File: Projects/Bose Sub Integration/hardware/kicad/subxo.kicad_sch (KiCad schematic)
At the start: 44 parts, among them J1 IN L, J2 IN R, J3 OUT 3.5mm, J4 PWR IN 15V, J5 POLARITY SW, J6 LEVEL POT 10k, J7 INV LED, U1 TL074, U2 LM7812

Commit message: Sub crossover: redraw the schematic so it can be read
The schematic was electrically correct and visually useless: every one of its
112 wires was exactly 2.54 mm, one stub per pin, each ending in a net label.
Nothing was drawn as a connection, so tracing a net meant text-searching the
sheet, and the Sallen-Key and the op-amp stages were unrecognisable.

Redrawn in blocks with real wires, ground symbols and drawn feedback loops:
power in, status LEDs and virtual ground across the top; inputs, summing,
Sallen-Key and polarity inverter through the middle; output stage and the tied
-off spare section below.

The electrical design is untouched and provably so - the netlist partition,
all 44 parts, 31 nets and 112 nodes, is identical, and Value/Footprint are
copied from the old sheet rather than retyped. Net names are preserved too,
since the PCB matches on them; the one exception is /GND -> GND, because
ground moved from a text label onto proper power symbols.

  stitched pins   97% -> 8%       median wire  2.54 mm -> 10.16 mm
  wired pins      13% -> 92%      junctions          0 -> 34
  ERC violations     9 -> 5       ground symbols     0 -> 9

tools/subxo_layout.py regenerates the sheet, so the drawing is reproducible.
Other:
- note added: "A POWER IN +15 V -> LM7812 -> +12 V"
- note added: "An unterminated spare section oscillates and couples into its neighbours through the shared supply."
- note added: "B STATUS LEDS"
- note added: "C VIRTUAL GROUND +6 V, buffered"
- note added: "D INPUTS L + R, DC-blocked, summed"
- note added: "D2 is lit from J7 by the polarity switch's spare pole."
- note added: "E SALLEN-KEY LOW-PASS 2nd order"
- note added: "F POLARITY INVERTER unity gain -1"
- note added: "G OUTPUT polarity select -> level -> jack"
- note added: "H SPARE SECTION tied off, not floating"
- note added: "JP1/JP2 select C1 and C2 independently -- nine corners, not three."
- note added: "LK1 is the single tie between supply return and signal ground."
- note added: "R7 + JP3 let the output shield be damped or lifted at the jack."
- note added: "R_b1/R_b2 are the only DC path to U1A's + input -- without them the amp drifts to a rail."
- note added: "U1 supply: pin 4 = V12, pin 11 = GND."
- note removed: "A POWER IN -> +12 V"
- note removed: "A4 is the spare section: + on VGND, out tied to in-. An unterminated spare oscillates and couples into its neighbours through the shared supply."
- note removed: "B U1 SUPPLY"
- note removed: "Bose Companion 5 sub crossover -- mono-summing 2nd-order Sallen-Key low-pass."
- note removed: "C VIRTUAL GROUND 6 V"
- note removed: "C1 returns to N1 -- the Sallen-Key feedback path. Not N2. JP1 selects C1 (odd pin = cap, even pin = N1); JP2 selects C2 (odd = cap, even = VGND). They select INDEPENDENTLY -- nine corners, not three pairs. Corners below are MEASURED on the rev A board, not calculated: the quoted f0 = 1/(2*pi*R*sqrt(C1*C2)) is not a -3 dB point, and C_in sits inside the filter. See Results - Sub Crossover Bring-up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"
- note removed: "C_in1/C_in2 use a dual-pitch footprint: 5.00 mm for the 220n as built (or a 2u2 non-polarised electrolytic), 15.00 mm for a real 2u2 film part. Fit ONE pair. 220n puts ~8.8k of reactance in series with R1 at 82 Hz, so it is part of the filter, not just an input high-pass -- it costs 1.3-3.1 dB of passband level and damps the peaking. Whether that is a defect or a feature is a listening question; 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"
- note removed: "C_out + faces SW_COM: that node sits at 6 V DC, the pot side at 0 V. J6 pin 3 = GND, not VGND -- C_out has already removed the 6 V bias; referencing the pot to VGND would thump the driver at power-on. JP3 shorts R7 (ground lift). Normally fitted."
- note removed: "D INPUT L"
- note removed: "D1 = power lamp on V12 (proves the LM7812, not just VIN). D2 = INVERTED lamp, fed from SW2's unused second pole via J7. Both ~2 mA. No LED touches a signal node."
- note removed: "E INPUT R"
- note removed: "F SALLEN-KEY LOW-PASS"
- note removed: "G POLARITY INVERTER"
- note removed: "H OUTPUT STAGE"
- note removed: "I STATUS LEDS"
- note removed: "Off-board: level pot (J6), polarity switch (J5), all panel jacks (J1/J2/J3). Process: single-sided THT, bottom copper only, board outline 100 x 100 mm. Copper is isolation-milled on the CNC with an 0.8 mm flat end mill; the fiber laser does the silkscreen only. Routing clearance 0.85 mm / track 1.0 mm. The 0.8 mm tool width is a hard floor on every copper-to-copper gap. Fixed-pitch pads sit below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"
- note removed: "R_b1/R_b2 are the only DC path to A1's + input (C_in blocks DC, C2 is a capacitor). Without them A1 drifts to a rail. They sit after the coupling caps -- 100k at N1 would shift every corner by 8%."
- note removed: "Reference names vs the handoff document: KiCad treats a reference with no trailing digit as unannotated, so C1a/C1b/C1c -> C1_1/C1_2/C1_3, C2a/C2b/C2c -> C2_1/C2_2/C2_3, R1a/R1b -> R1_1/R1_2, C_out -> C_out1."
- note removed: "Single +12 V rail, no negative supply. All AC referenced to VGND = 6 V (A3 buffers the R8/R9 mid-rail divider)."
- note removed: "U1 supply: pin 4 = V12, pin 11 = GND. No negative rail."

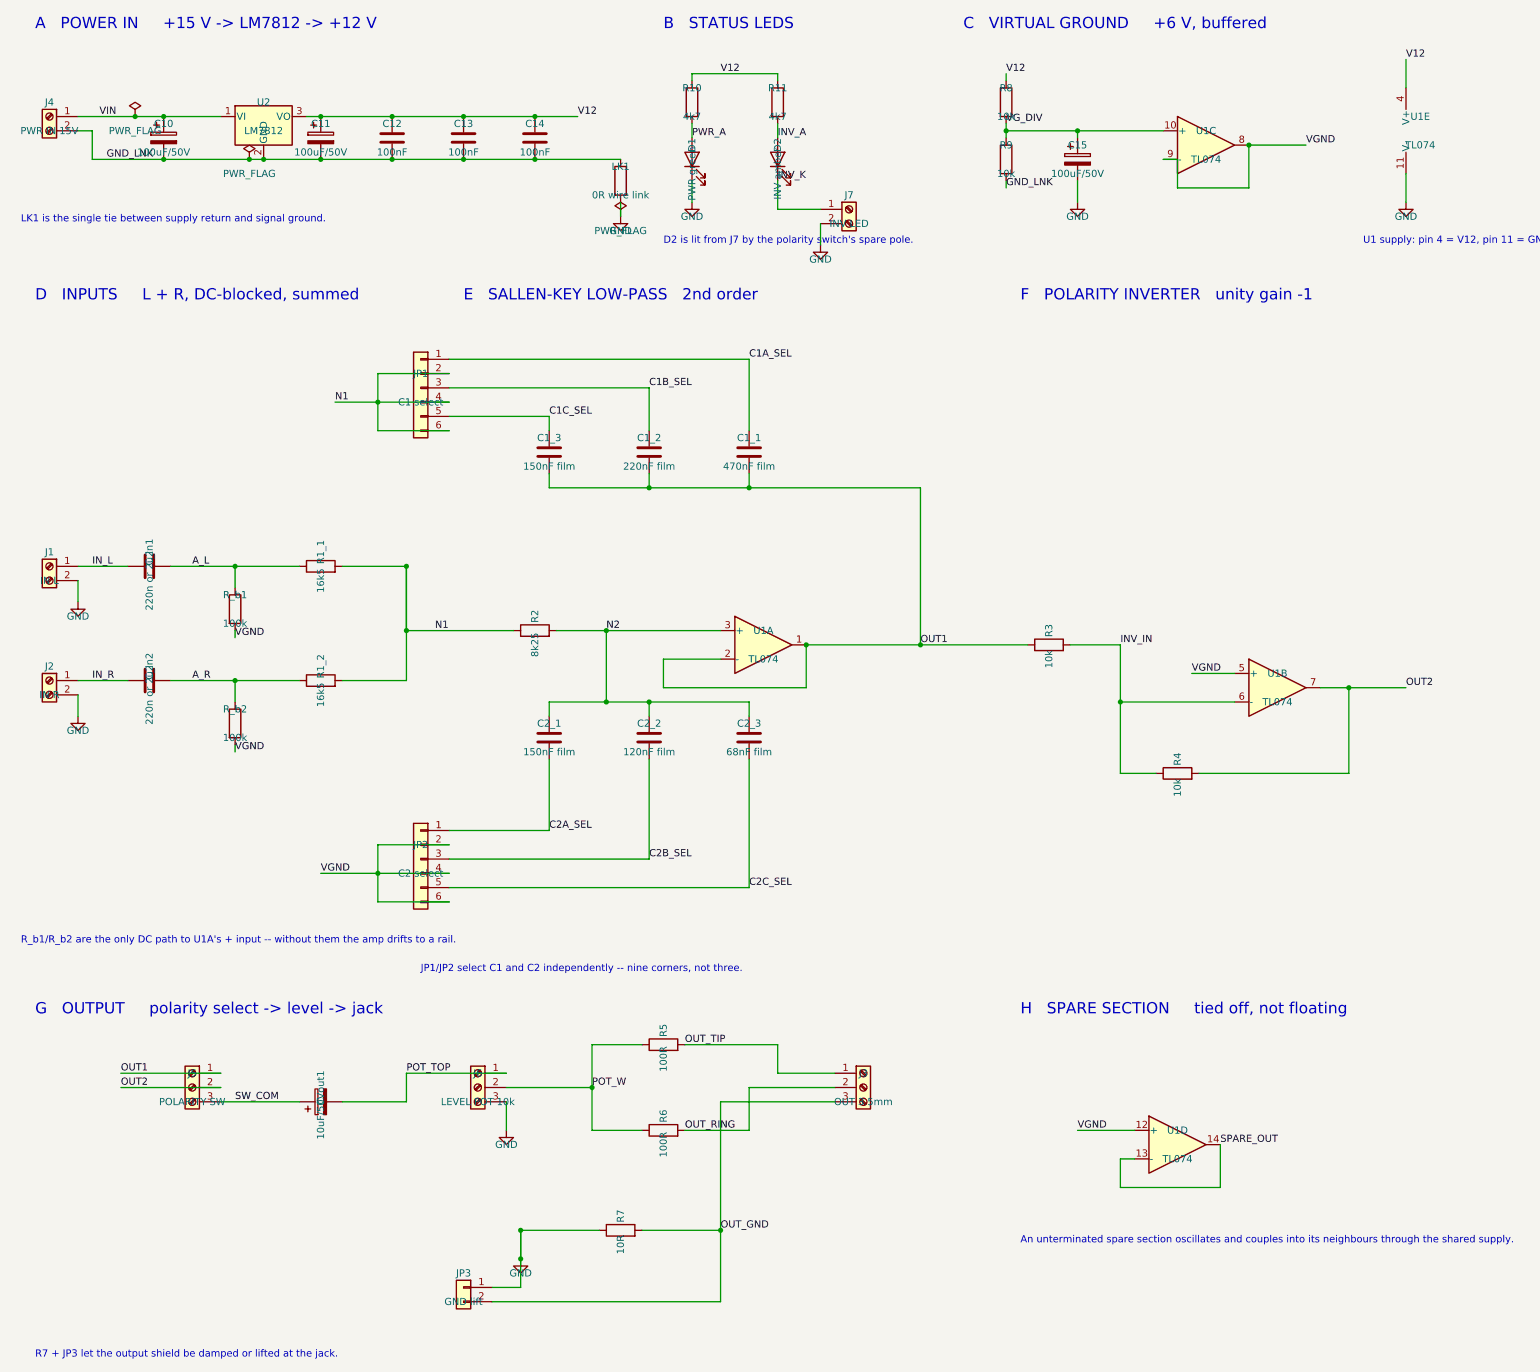
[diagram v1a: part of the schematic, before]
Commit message: Sub crossover: keep the field text off the part bodies
The emitter pinned every Reference and Value 2.54 mm above and below the symbol
origin regardless of the part's shape, so on vertical resistors and capacitors,
and inside connector bodies, the text was drawn straight through the symbol.
Field positions now come from the part's own bounding box: beside a tall part,
above and below a wide one.

Netlist unchanged - still identical to the pre-redraw sheet at 44 parts,
31 nets and 112 nodes, ERC still 5 violations.
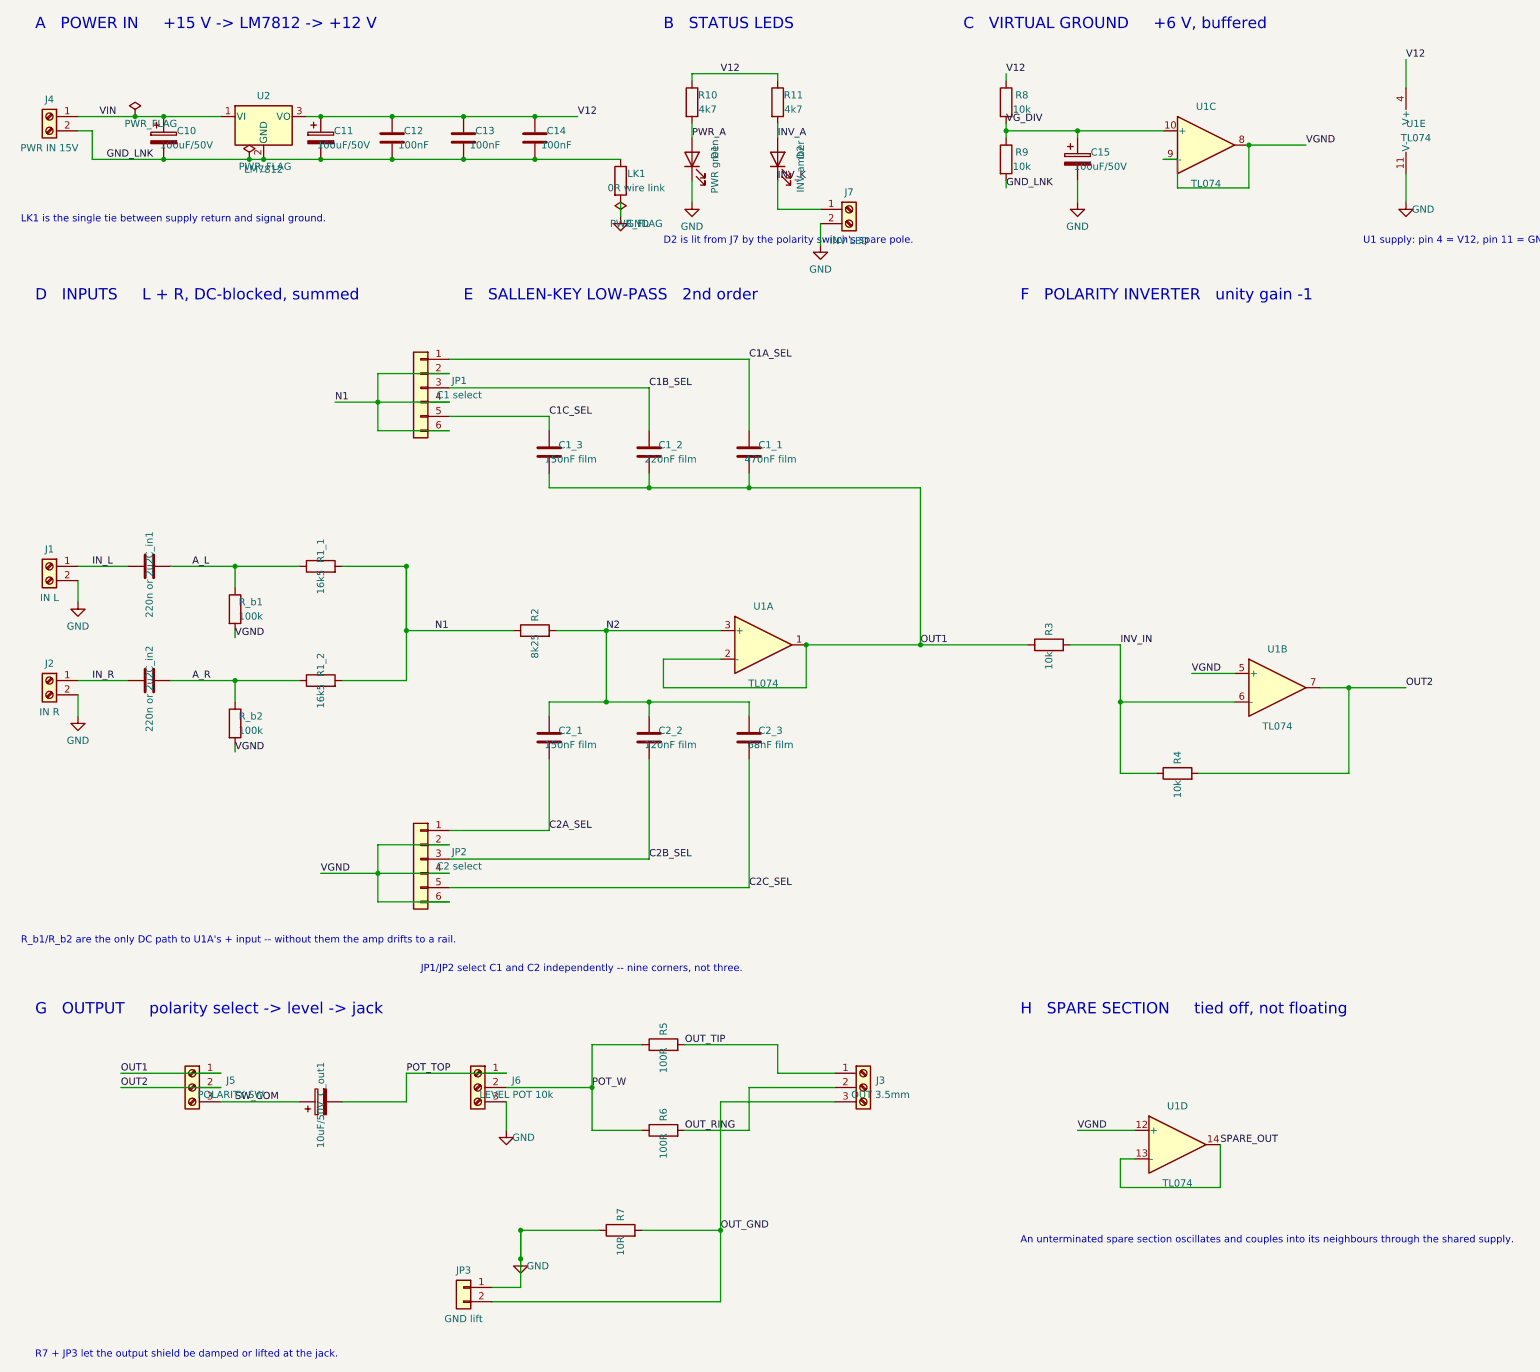
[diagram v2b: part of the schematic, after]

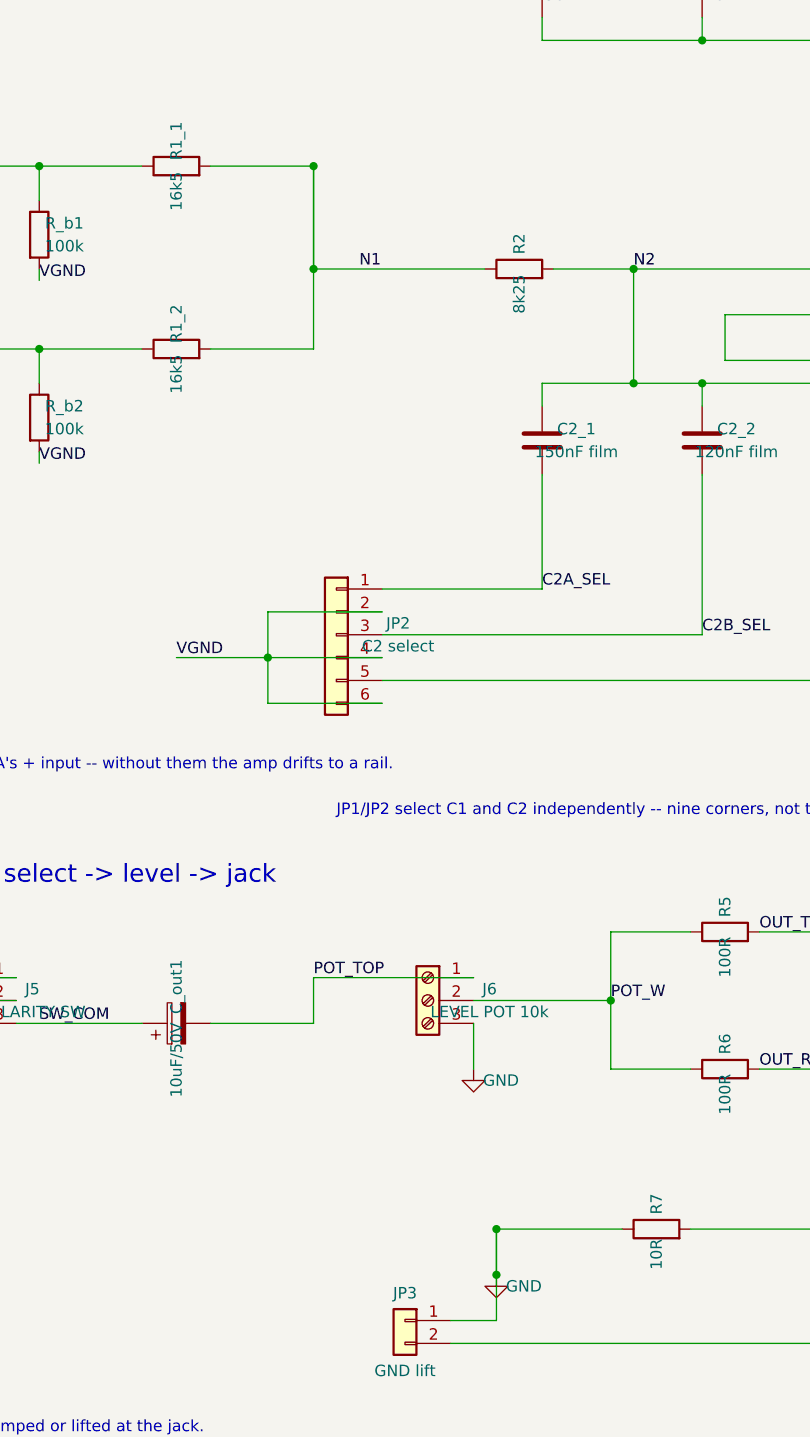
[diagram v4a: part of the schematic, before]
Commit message: Sub crossover: write the sheet through KiCad's own writer
The emitted file put each lib_symbols entry on one 1600-character line. That
is valid s-expression and kicad-cli reads it perfectly, but it is not the
format KiCad writes, and the GUI was reporting unconnected pins that neither
the netlister nor the CLI's ERC could see.

Passing the file through "kicad-cli sch upgrade --force" re-saves it in
KiCad's canonical form - 6018 lines becomes 9515 - so what ships is what
KiCad itself would have written. Structure is unchanged: 148 wires, 33
junctions, no pin left sitting on a wire's interior, netlist identical at
44 parts / 31 nets / 112 nodes, ERC --severity-all back to 5
lib_symbol_mismatch.

Also deduplicates two identical wire segments the splitting pass emitted.
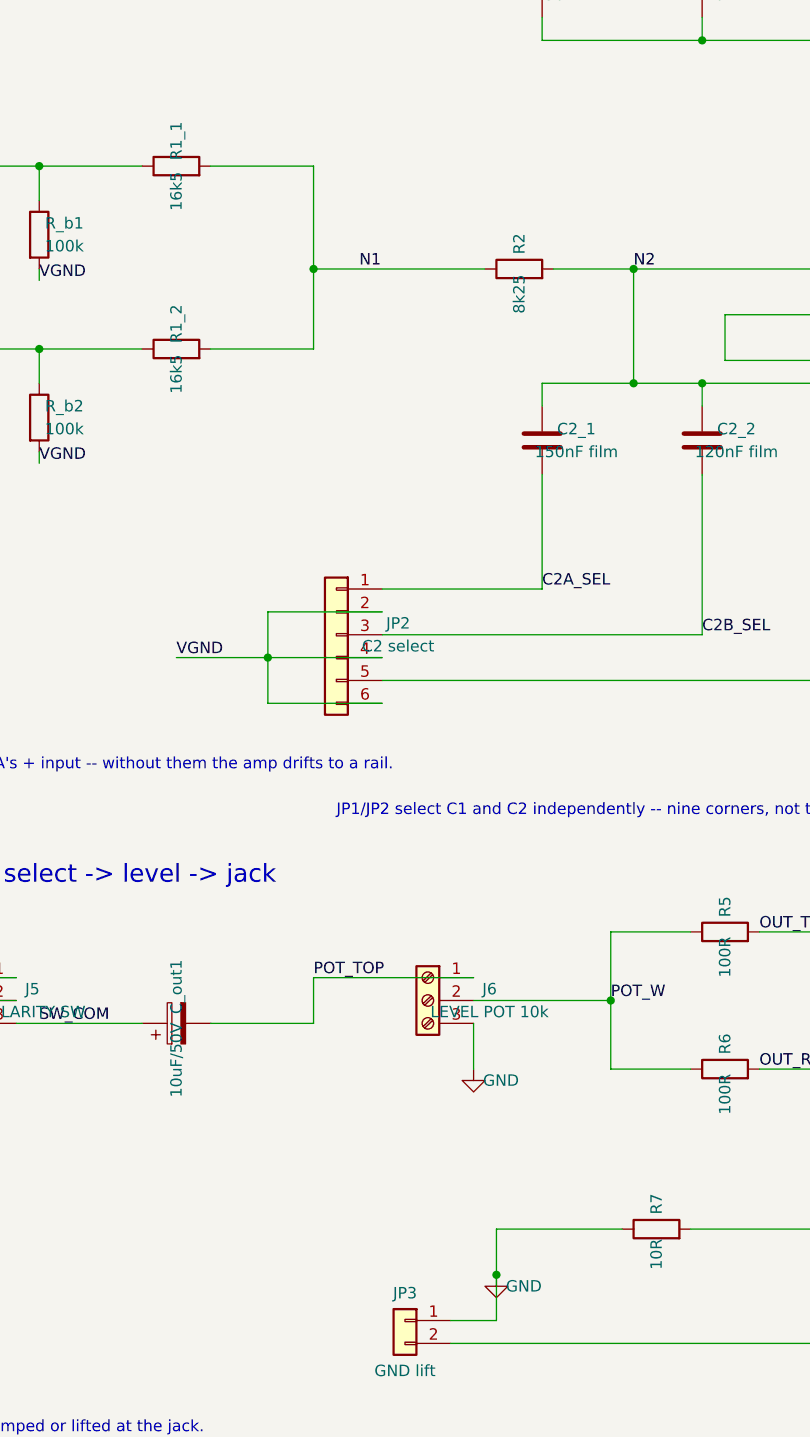
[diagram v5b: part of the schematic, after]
